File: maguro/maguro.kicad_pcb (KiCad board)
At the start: 2 copper layers, 114.3 x 69.8 mm, 21 parts, among them SW1001 SW_Push, SW1101 SW_Push, SW1301 SW_Push, SW1401 SW_Push, SW301 SW_Push, SW401 SW_Push, SW501 SW_Push, SW601 SW_Push, SW801 SW_Push, SW901 SW_Push

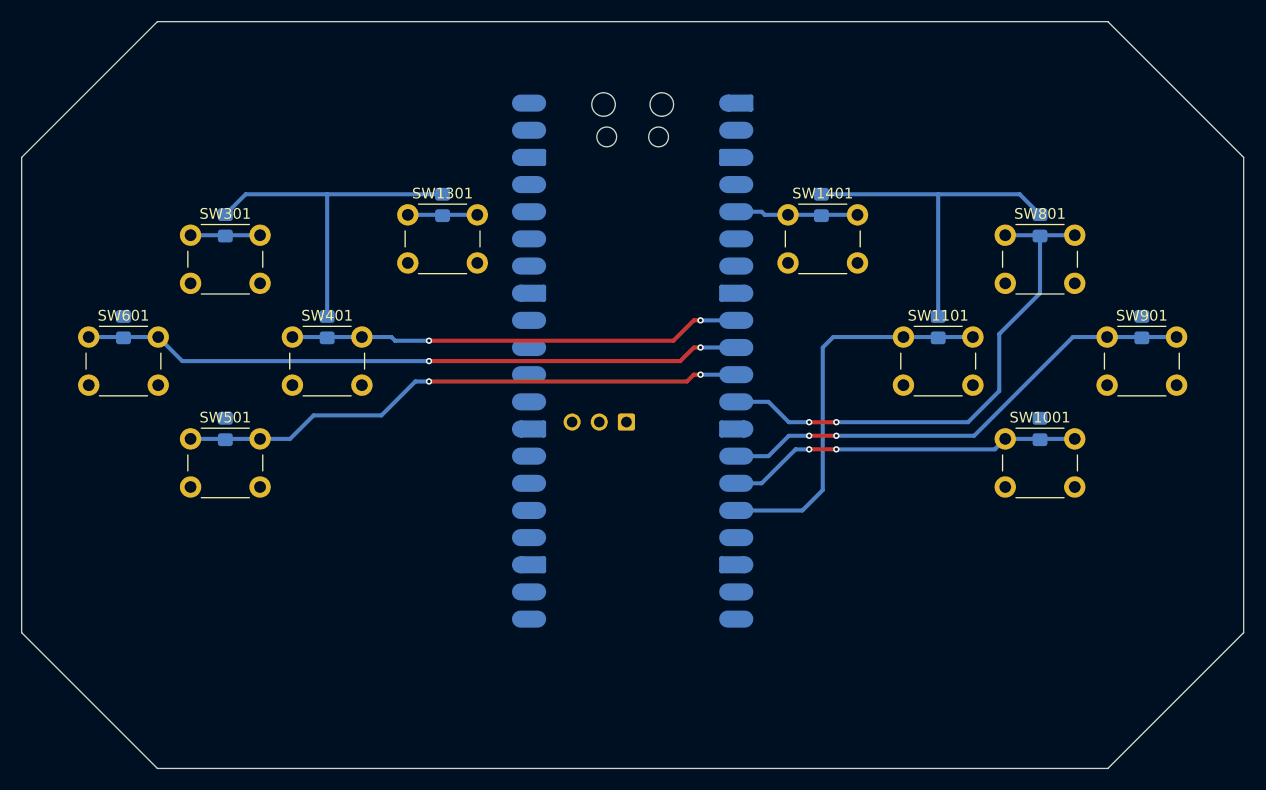
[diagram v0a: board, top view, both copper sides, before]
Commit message: Pushed buttons to top
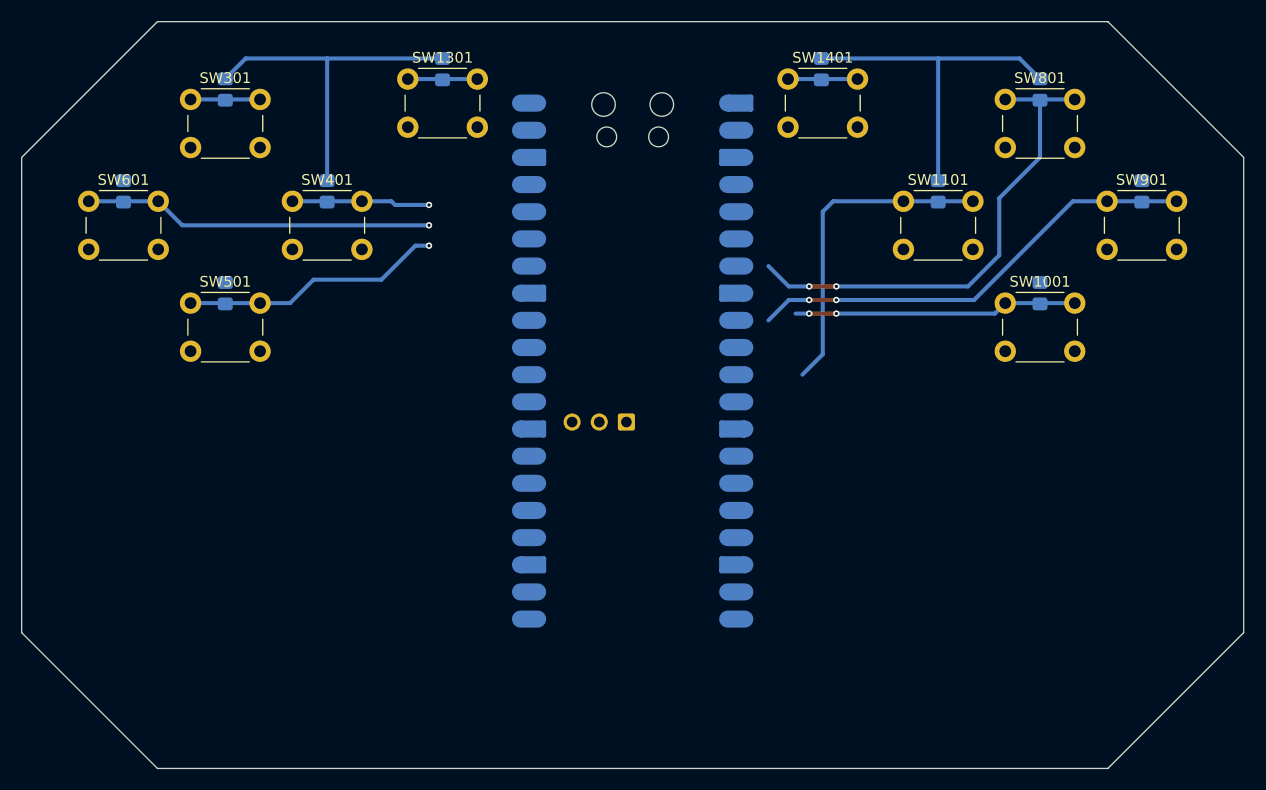
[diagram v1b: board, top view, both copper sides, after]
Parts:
- moved R1001 12.7 mm to (177.8, 95.2)
- moved R1101 12.7 mm to (168.3, 85.7)
- moved R1301 12.7 mm to (121.9, 74.3)
- moved R1401 12.7 mm to (157.4, 74.3)
- moved R301 12.7 mm to (101.6, 76.2)
- moved R401 12.7 mm to (111.1, 85.7)
- moved R501 12.7 mm to (101.6, 95.2)
- moved R601 12.7 mm to (92.1, 85.7)
- moved R801 12.7 mm to (177.8, 76.2)
- moved R901 12.7 mm to (187.3, 85.7)
- moved SW1001 12.7 mm to (174.6, 96.2)
- moved SW1301 12.7 mm to (118.7, 75.2)
- moved SW1401 12.7 mm to (154.2, 75.2)
- moved SW301 12.7 mm to (98.3, 77.1)
- moved SW501 12.7 mm to (98.3, 96.2)
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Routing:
- net /dpad_right: track 42.4 -> 12.9 mm, vias 2 -> 1
- net /dpad_down: track 62.1 -> 32.8 mm, vias 2 -> 1
- net /dpad_left: track 53.5 -> 24.5 mm, vias 2 -> 1
- net /button_b: track 33.4 -> 26.5 mm
- net /button_y: track 36.7 -> 30.5 mm
- net /button_select: track 11.5 -> 6.50 mm
- net /button_a: track 45.9 -> 42.9 mm
- net /button_x: track 49.2 -> 46.2 mm

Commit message: Added joysticks
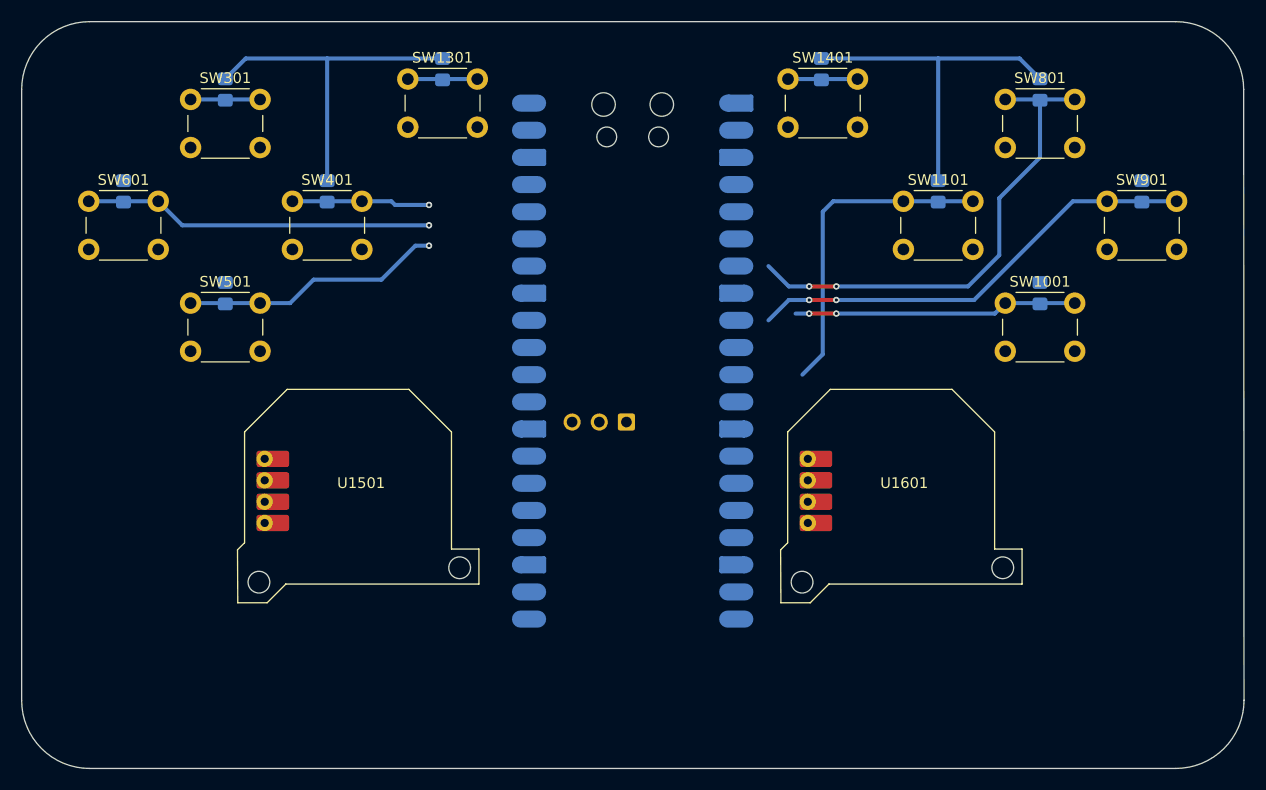
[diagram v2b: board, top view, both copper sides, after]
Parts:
- added U1501: ~, osdb:COM-09426, F.Cu at (114.3, 114.3)
- added U1601: ~, osdb:COM-09426, F.Cu at (165.1, 114.3)
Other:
- outline, holes or cut-outs redrawn
